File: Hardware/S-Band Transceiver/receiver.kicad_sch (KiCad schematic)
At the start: 70 parts, among them J6 SMA-J-P-H-ST-EM1, J7 SMA-J-P-H-ST-EM1, J8 SMA-J-P-H-ST-EM1, U13 LT1819, U14 LT1819, U15 ADL5380, U16 TSS-53LNB3+, U17 SN74LVC1G125DBVR, U18 SKY16603-632LF, U19 DCW-22-332+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

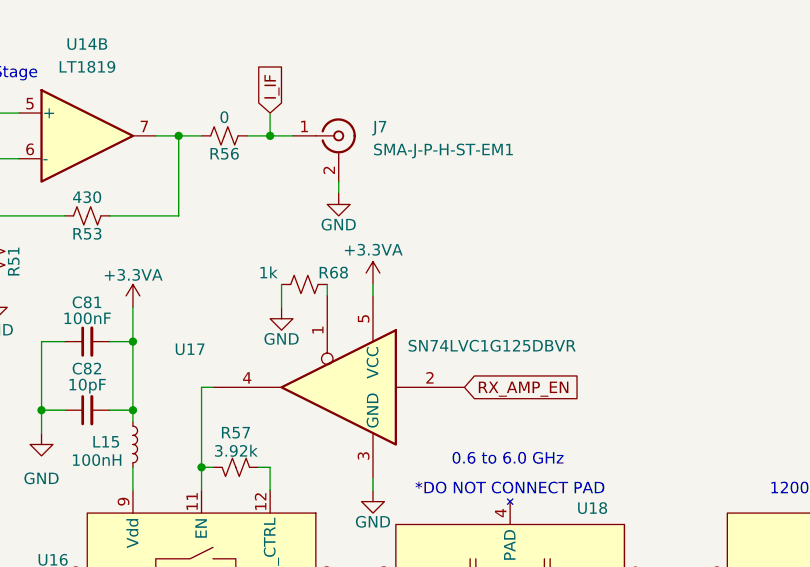
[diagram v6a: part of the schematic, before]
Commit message: Adding decoupling capacitor
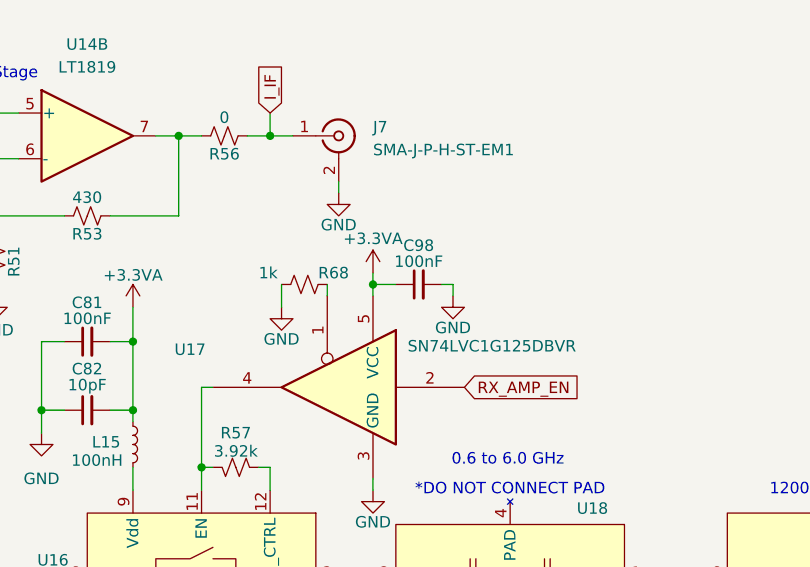
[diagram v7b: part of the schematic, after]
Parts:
- added C98: 100nF, Capacitor_SMD:C_0402_1005Metric, symbol Device:C_Small
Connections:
- net +3.3VA: now also C98.1
- net GND: now also C98.2
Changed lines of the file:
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@@
 	)
 	(junction
+		(at 153.67 49.53)
+		(diameter 0)
+		(color 0 0 0 0)
+	)
+	(junction
 		(at 40.64 132.08)
 		(diameter 0)
@@
 	(wire
 		(pts
+			(xy 153.67 49.53) (xy 156.21 49.53)
+		)
+		(stroke
+			(width 0)
+			(type default)
+		)
+	)
+	(wire
+		(pts
 			(xy 101.6 123.19) (xy 101.6 127)
 		)
@@
 	(wire
 		(pts
+			(xy 153.67 49.53) (xy 153.67 50.8)
+		)
+		(stroke
+			(width 0)
+			(type default)
+		)
+	)
+	(wire
+		(pts
 			(xy 240.03 106.68) (xy 241.3 106.68)
 		)
@@
 	(wire
 		(pts
-			(xy 153.67 49.53) (xy 153.67 50.8)
+			(xy 153.67 48.26) (xy 153.67 49.53)
 		)
 		(stroke
@@
 	(wire
 		(pts
+			(xy 162.56 49.53) (xy 162.56 50.8)
+		)
+		(stroke
+			(width 0)
+			(type default)
+		)
+	)
+	(wire
+		(pts
 			(xy 161.29 137.16) (xy 161.29 138.43)
 		)
@@
 	(wire
 		(pts
+			(xy 161.29 49.53) (xy 162.56 49.53)
+		)
+		(stroke
+			(width 0)
+			(type default)
+		)
+	)
+	(wire
+		(pts
 			(xy 40.64 149.86) (xy 43.18 149.86)
 		)
@@
 	(symbol
 		(lib_id "power:+3.3VA")
-		(at 153.67 49.53 0)
+		(at 153.67 48.26 0)
 		(mirror y)
 		(unit 1)
@@
 		(dnp no)
 		(property "Reference" "#PWR0121"
-			(at 153.67 53.34 0)
+			(at 153.67 52.07 0)
 			(effects
 				(font
@@
 		)
 		(property "Value" "+3.3VA"
-			(at 153.67 45.72 0)
+			(at 153.67 44.45 0)
 			(effects
 				(font
@@
 		)
 		(property "Footprint" ""
-			(at 153.67 49.53 0)
+			(at 153.67 48.26 0)
 			(effects
 				(font
@@
 		)
 		(property "Datasheet" ""
-			(at 153.67 49.53 0)
+			(at 153.67 48.26 0)
 			(effects
 				(font
@@
 		)
 		(property "Description" "Power symbol creates a global label with name \"+3.3VA\""
-			(at 153.67 49.53 0)
+			(at 153.67 48.26 0)
 			(effects
 				(font
@@
 	)
 	(symbol
+		(lib_id "Device:C_Small")
+		(at 158.75 49.53 90)
+		(unit 1)
+		(exclude_from_sim no)
+		(in_bom yes)
+		(on_board yes)
+		(dnp no)
+		(property "Reference" "C98"
+			(at 158.75 45.212 90)
+			(effects
+				(font
+					(size 1.27 1.27)
+				)
+			)
+		)
+		(property "Value" "100nF"
+			(at 158.75 46.99 90)
+			(effects
+				(font
+					(size 1.27 1.27)
+				)
+			)
+		)
+		(property "Footprint" "Capacitor_SMD:C_0402_1005Metric"
+			(at 158.75 49.53 0)
+			(effects
+				(font
+					(size 1.27 1.27)
+				)
+				(hide yes)
+			)
+		)
+		(property "Datasheet" "~"
+			(at 158.75 49.53 0)
+			(effects
+				(font
+					(size 1.27 1.27)
+				)
+				(hide yes)
+			)
+		)
+		(property "Description" "Unpolarized capacitor, small symbol"
+			(at 158.75 49.53 0)
+			(effects
+				(font
+					(size 1.27 1.27)
+				)
+				(hide yes)
+			)
+		)
+		(pin "2"
+		)
+		(pin "1"
+		)
+		(instances
+			(project "S-Band Transceiver"
+				(path "/811f57cf-e3df-4fba-aff9-353adc85299e/f050a99f-ee17-49d7-ba1b-b225c3b6208d"
+					(reference "C98")
+					(unit 1)
+				)
+			)
+		)
+	)
+	(symbol
 		(lib_id "power:+5V")
 		(at 40.64 130.81 0)
@@
 					(unit 1)
 				)
+			)
+		)
+	)
+	(symbol
+		(lib_id "power:GND")
+		(at 162.56 50.8 0)
+		(unit 1)
+		(exclude_from_sim no)
+		(in_bom yes)
+		(on_board yes)
+		(dnp no)
+		(property "Reference" "#PWR0146"
+			(at 162.56 57.15 0)
+			(effects
+				(font
+					(size 1.27 1.27)
+				)
+				(hide yes)
+			)
+		)
+		(property "Value" "GND"
+			(at 162.56 54.356 0)
+			(effects
+				(font
+					(size 1.27 1.27)
+				)
+			)
+		)
+		(property "Footprint" ""
+			(at 162.56 50.8 0)
+			(effects
+				(font
+					(size 1.27 1.27)
+				)
+				(hide yes)
+			)
+		)
+		(property "Datasheet" ""
+			(at 162.56 50.8 0)
+			(effects
+				(font
+					(size 1.27 1.27)
+				)
+				(hide yes)
+			)
+		)
+		(property "Description" "Power symbol creates a global label with name \"GND\" , ground"
+			(at 162.56 50.8 0)
+			(effects
+				(font
+					(size 1.27 1.27)
+				)
+				(hide yes)
+			)
+		)
+		(pin "1"
+		)
+		(instances
+			(project "S-Band Transceiver"
+				(path "/811f57cf-e3df-4fba-aff9-353adc85299e/f050a99f-ee17-49d7-ba1b-b225c3b6208d"
+					(reference "#PWR0146")
+					(unit 1)
+				)
